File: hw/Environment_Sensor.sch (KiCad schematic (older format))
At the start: 30 parts, among them P1 CONN_4, P2 CONN_4, U1 MCP1703T, U2 PCA9512ADP, U3 TMP105, U4 HIH-6131-021, U5 MPL115A, U6 TSL2561T, U7 HTU21D

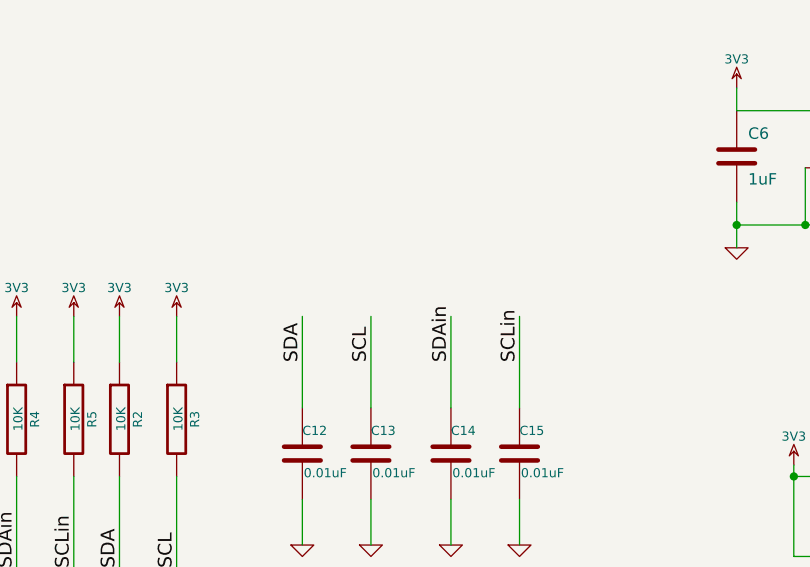
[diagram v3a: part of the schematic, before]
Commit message: Updated to add the caps on to the SDA/SCL lines
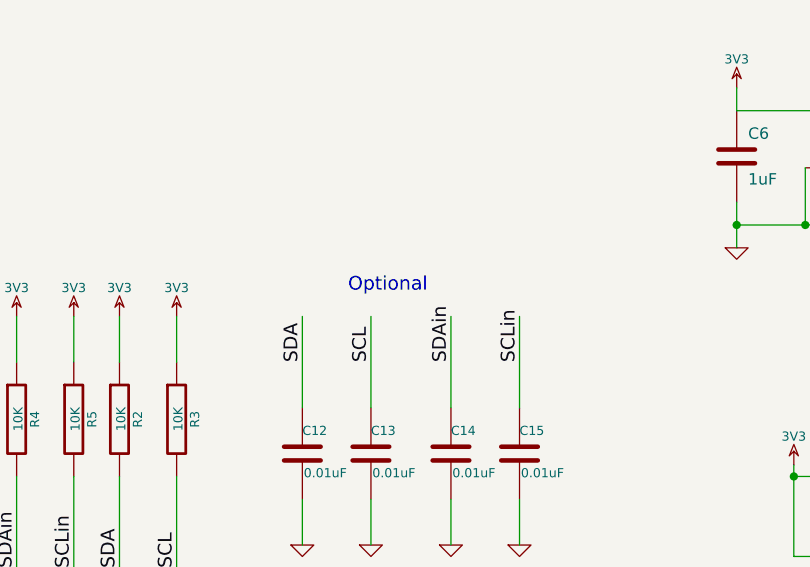
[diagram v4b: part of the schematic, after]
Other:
- note added: "Optional"
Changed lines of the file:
@@
 	5200 1650 5200 1550
 $Comp
-L +5V #PWR22
+L +5V #PWR01
 U 1 1 53729ED8
 P 5200 1550
-F 0 "#PWR22" H 5200 1640 20  0001 C CNN
+F 0 "#PWR01" H 5200 1640 20  0001 C CNN
 F 1 "+5V" H 5200 1640 30  0000 C CNN
 F 2 "" H 5200 1550 60  0001 C CNN
@@
 $EndComp
 $Comp
-L PWR_FLAG #FLG1
+L PWR_FLAG #FLG02
 U 1 1 53729EC8
 P 5200 1650
-F 0 "#FLG1" H 5200 1745 30  0001 C CNN
+F 0 "#FLG02" H 5200 1745 30  0001 C CNN
 F 1 "PWR_FLAG" H 5200 1830 30  0000 C CNN
 F 2 "" H 5200 1650 60  0001 C CNN
@@
 SDA
 $Comp
-L 3V3 #PWR28
+L 3V3 #PWR03
 U 1 1 5372962B
 P 6750 2850
-F 0 "#PWR28" H 6750 2950 40  0001 C CNN
+F 0 "#PWR03" H 6750 2950 40  0001 C CNN
 F 1 "3V3" H 6750 2975 40  0000 C CNN
 F 2 "" H 6750 2850 60  0001 C CNN
@@
 $EndComp
 $Comp
-L GND #PWR26
+L GND #PWR04
 U 1 1 537295E4
 P 6350 3350
-F 0 "#PWR26" H 6350 3350 30  0001 C CNN
+F 0 "#PWR04" H 6350 3350 30  0001 C CNN
 F 1 "GND" H 6350 3280 30  0001 C CNN
 F 2 "" H 6350 3350 60  0001 C CNN
@@
 $EndComp
 $Comp
-L 3V3 #PWR16
+L 3V3 #PWR05
 U 1 1 53729235
 P 4650 2950
-F 0 "#PWR16" H 4650 3050 40  0001 C CNN
+F 0 "#PWR05" H 4650 3050 40  0001 C CNN
 F 1 "3V3" H 4650 3075 40  0000 C CNN
 F 2 "" H 4650 2950 60  0001 C CNN
@@
 $EndComp
 $Comp
-L GND #PWR17
+L GND #PWR06
 U 1 1 5372922C
 P 4650 3500
-F 0 "#PWR17" H 4650 3500 30  0001 C CNN
+F 0 "#PWR06" H 4650 3500 30  0001 C CNN
 F 1 "GND" H 4650 3430 30  0001 C CNN
 F 2 "" H 4650 3500 60  0001 C CNN
@@
 $EndComp
 $Comp
-L GND #PWR19
+L GND #PWR07
 U 1 1 53729228
 P 4850 3450
-F 0 "#PWR19" H 4850 3450 30  0001 C CNN
+F 0 "#PWR07" H 4850 3450 30  0001 C CNN
 F 1 "GND" H 4850 3380 30  0001 C CNN
 F 2 "" H 4850 3450 60  0001 C CNN
@@
 SDA
 $Comp
-L 3V3 #PWR10
+L 3V3 #PWR08
 U 1 1 53728CA5
 P 3400 7400
-F 0 "#PWR10" H 3400 7500 40  0001 C CNN
+F 0 "#PWR08" H 3400 7500 40  0001 C CNN
 F 1 "3V3" H 3400 7525 40  0000 C CNN
 F 2 "" H 3400 7400 60  0001 C CNN
@@
 $EndComp
 $Comp
-L 3V3 #PWR1
+L 3V3 #PWR09
 U 1 1 53728C52
 P 1350 6350
-F 0 "#PWR1" H 1350 6450 40  0001 C CNN
+F 0 "#PWR09" H 1350 6450 40  0001 C CNN
 F 1 "3V3" H 1350 6475 40  0000 C CNN
 F 2 "" H 1350 6350 60  0001 C CNN
@@
 $EndComp
 $Comp
-L GND #PWR13
+L GND #PWR010
 U 1 1 53728C4C
 P 3850 6850
-F 0 "#PWR13" H 3850 6850 30  0001 C CNN
+F 0 "#PWR010" H 3850 6850 30  0001 C CNN
 F 1 "GND" H 3850 6780 30  0001 C CNN
 F 2 "" H 3850 6850 60  0001 C CNN
@@
 $EndComp
 $Comp
-L GND #PWR6
+L GND #PWR011
 U 1 1 53728C0A
 P 2000 6750
-F 0 "#PWR6" H 2000 6750 30  0001 C CNN
+F 0 "#PWR011" H 2000 6750 30  0001 C CNN
 F 1 "GND" H 2000 6680 30  0001 C CNN
 F 2 "" H 2000 6750 60  0001 C CNN
@@
 $EndComp
 $Comp
-L +5V #PWR14
+L +5V #PWR012
 U 1 1 53728BED
 P 3950 6350
-F 0 "#PWR14" H 3950 6440 20  0001 C CNN
+F 0 "#PWR012" H 3950 6440 20  0001 C CNN
 F 1 "+5V" H 3950 6440 30  0000 C CNN
 F 2 "" H 3950 6350 60  0001 C CNN
@@
 $EndComp
 $Comp
-L GND #PWR2
+L GND #PWR013
 U 1 1 53728BD6
 P 1550 6850
-F 0 "#PWR2" H 1550 6850 30  0001 C CNN
+F 0 "#PWR013" H 1550 6850 30  0001 C CNN
 F 1 "GND" H 1550 6780 30  0001 C CNN
 F 2 "" H 1550 6850 60  0001 C CNN
@@
 $EndComp
 $Comp
-L +5V #PWR3
+L +5V #PWR014
 U 1 1 537288EE
 P 1700 3850
-F 0 "#PWR3" H 1700 3940 20  0001 C CNN
+F 0 "#PWR014" H 1700 3940 20  0001 C CNN
 F 1 "+5V" H 1700 3940 30  0000 C CNN
 F 2 "" H 1700 3850 60  0001 C CNN
@@
 $EndComp
 $Comp
-L 3V3 #PWR12
+L 3V3 #PWR015
 U 1 1 537288E9
 P 3500 3900
-F 0 "#PWR12" H 3500 4000 40  0001 C CNN
+F 0 "#PWR015" H 3500 4000 40  0001 C CNN
 F 1 "3V3" H 3500 4025 40  0000 C CNN
 F 2 "" H 3500 3900 60  0001 C CNN
@@
 $EndComp
 $Comp
-L GND #PWR5
+L GND #PWR016
 U 1 1 537288DE
 P 1950 4350
-F 0 "#PWR5" H 1950 4350 30  0001 C CNN
+F 0 "#PWR016" H 1950 4350 30  0001 C CNN
 F 1 "GND" H 1950 4280 30  0001 C CNN
 F 2 "" H 1950 4350 60  0001 C CNN
@@
 $EndComp
 $Comp
-L GND #PWR8
+L GND #PWR017
 U 1 1 537288D9
 P 2600 4550
-F 0 "#PWR8" H 2600 4550 30  0001 C CNN
+F 0 "#PWR017" H 2600 4550 30  0001 C CNN
 F 1 "GND" H 2600 4480 30  0001 C CNN
 F 2 "" H 2600 4550 60  0001 C CNN
@@
 $EndComp
 $Comp
-L 3V3 #PWR36
+L 3V3 #PWR018
 U 1 1 5372789B
 P 8150 5300
-F 0 "#PWR36" H 8150 5400 40  0001 C CNN
+F 0 "#PWR018" H 8150 5400 40  0001 C CNN
 F 1 "3V3" H 8150 5425 40  0000 C CNN
 F 2 "" H 8150 5300 60  0001 C CNN
@@
 $EndComp
 $Comp
-L 3V3 #PWR31
+L 3V3 #PWR019
 U 1 1 53727880
 P 7550 4500
-F 0 "#PWR31" H 7550 4600 40  0001 C CNN
+F 0 "#PWR019" H 7550 4600 40  0001 C CNN
 F 1 "3V3" H 7550 4625 40  0000 C CNN
 F 2 "" H 7550 4500 60  0001 C CNN
@@
 $EndComp
 $Comp
-L GND #PWR32
+L GND #PWR020
 U 1 1 5372787B
 P 7550 5200
-F 0 "#PWR32" H 7550 5200 30  0001 C CNN
+F 0 "#PWR020" H 7550 5200 30  0001 C CNN
 F 1 "GND" H 7550 5130 30  0001 C CNN
 F 2 "" H 7550 5200 60  0001 C CNN
@@
 NoConn ~ 9700 5100
 $Comp
-L GND #PWR30
+L GND #PWR021
 U 1 1 537277D0
 P 7400 3500
-F 0 "#PWR30" H 7400 3500 30  0001 C CNN
+F 0 "#PWR021" H 7400 3500 30  0001 C CNN
 F 1 "GND" H 7400 3430 30  0001 C CNN
 F 2 "" H 7400 3500 60  0001 C CNN
@@
 $EndComp
 $Comp
-L 3V3 #PWR29
+L 3V3 #PWR022
 U 1 1 537277C9
 P 7400 2800
-F 0 "#PWR29" H 7400 2900 40  0001 C CNN
+F 0 "#PWR022" H 7400 2900 40  0001 C CNN
 F 1 "3V3" H 7400 2925 40  0000 C CNN
 F 2 "" H 7400 2800 60  0001 C CNN
@@
 $EndComp
 $Comp
-L 3V3 #PWR33
+L 3V3 #PWR023
 U 1 1 53727546
 P 7800 6150
-F 0 "#PWR33" H 7800 6250 40  0001 C CNN
+F 0 "#PWR023" H 7800 6250 40  0001 C CNN
 F 1 "3V3" H 7800 6275 40  0000 C CNN
 F 2 "" H 7800 6150 60  0001 C CNN
@@
 $EndComp
 $Comp
-L GND #PWR37
+L GND #PWR024
 U 1 1 5372753A
 P 8300 6600
-F 0 "#PWR37" H 8300 6600 30  0001 C CNN
+F 0 "#PWR024" H 8300 6600 30  0001 C CNN
 F 1 "GND" H 8300 6530 30  0001 C CNN
 F 2 "" H 8300 6600 60  0001 C CNN
@@
 $EndComp
 $Comp
-L +5V #PWR4
+L +5V #PWR025
 U 1 1 53726FA2
 P 1900 2100
-F 0 "#PWR4" H 1900 2190 20  0001 C CNN
+F 0 "#PWR025" H 1900 2190 20  0001 C CNN
 F 1 "+5V" H 1900 2190 30  0000 C CNN
 F 2 "" H 1900 2100 60  0001 C CNN
@@
 $EndComp
 $Comp
-L GND #PWR7
+L GND #PWR026
 U 1 1 53726F75
 P 2200 2300
-F 0 "#PWR7" H 2200 2300 30  0001 C CNN
+F 0 "#PWR026" H 2200 2300 30  0001 C CNN
 F 1 "GND" H 2200 2230 30  0001 C CNN
 F 2 "" H 2200 2300 60  0001 C CNN
@@
 	3200 2150 3200 2100
 $Comp
-L +5V #PWR9
+L +5V #PWR027
 U 1 1 539395D4
 P 3200 2100
-F 0 "#PWR9" H 3200 2190 20  0001 C CNN
+F 0 "#PWR027" H 3200 2190 20  0001 C CNN
 F 1 "+5V" H 3200 2190 30  0000 C CNN
 F 2 "" H 3200 2100 60  0001 C CNN
@@
 $EndComp
 $Comp
-L GND #PWR11
+L GND #PWR028
 U 1 1 539395DA
 P 3500 2300
-F 0 "#PWR11" H 3500 2300 30  0001 C CNN
+F 0 "#PWR028" H 3500 2300 30  0001 C CNN
 F 1 "GND" H 3500 2230 30  0001 C CNN
 F 2 "" H 3500 2300 60  0001 C CNN
@@
 	8100 1800 8100 1900
 $Comp
-L GND #PWR35
+L GND #PWR029
 U 1 1 53BB120C
 P 8100 1900
-F 0 "#PWR35" H 8100 1900 30  0001 C CNN
+F 0 "#PWR029" H 8100 1900 30  0001 C CNN
 F 1 "GND" H 8100 1830 30  0001 C CNN
 F 2 "" H 8100 1900 60  0000 C CNN
@@
 $EndComp
 $Comp
-L 3V3 #PWR34
+L 3V3 #PWR030
 U 1 1 53BB122F
 P 8100 1350
-F 0 "#PWR34" H 8100 1450 40  0001 C CNN
+F 0 "#PWR030" H 8100 1450 40  0001 C CNN
 F 1 "3V3" H 8100 1475 40  0000 C CNN
 F 2 "" H 8100 1350 60  0000 C CNN
@@
 $EndComp
 $Comp
-L 3V3 #PWR20
+L 3V3 #PWR031
 U 1 1 53D97EA8
 P 4850 5500
-F 0 "#PWR20" H 4850 5600 40  0001 C CNN
+F 0 "#PWR031" H 4850 5600 40  0001 C CNN
 F 1 "3V3" H 4850 5625 40  0000 C CNN
 F 2 "" H 4850 5500 60  0000 C CNN
@@
 $EndComp
 $Comp
-L 3V3 #PWR21
+L 3V3 #PWR032
 U 1 1 53D97EBC
 P 5100 5500
-F 0 "#PWR21" H 5100 5600 40  0001 C CNN
+F 0 "#PWR032" H 5100 5600 40  0001 C CNN
 F 1 "3V3" H 5100 5625 40  0000 C CNN
 F 2 "" H 5100 5500 60  0000 C CNN
@@
 $EndComp
 $Comp
-L GND #PWR23
+L GND #PWR033
 U 1 1 53D98156
 P 5650 6500
-F 0 "#PWR23" H 5650 6500 30  0001 C CNN
+F 0 "#PWR033" H 5650 6500 30  0001 C CNN
 F 1 "GND" H 5650 6430 30  0001 C CNN
 F 2 "" H 5650 6500 60  0000 C CNN
@@
 $EndComp
 $Comp
-L GND #PWR24
+L GND #PWR034
 U 1 1 53D9816A
 P 5950 6500
-F 0 "#PWR24" H 5950 6500 30  0001 C CNN
+F 0 "#PWR034" H 5950 6500 30  0001 C CNN
 F 1 "GND" H 5950 6430 30  0001 C CNN
 F 2 "" H 5950 6500 60  0000 C CNN
@@
 $EndComp
 $Comp
-L GND #PWR25
+L GND #PWR035
 U 1 1 53D98312
 P 6300 6500
-F 0 "#PWR25" H 6300 6500 30  0001 C CNN
+F 0 "#PWR035" H 6300 6500 30  0001 C CNN
 F 1 "GND" H 6300 6430 30  0001 C CNN
 F 2 "" H 6300 6500 60  0000 C CNN
@@
 $EndComp
 $Comp
-L GND #PWR27
+L GND #PWR036
 U 1 1 53D98318
 P 6600 6500
-F 0 "#PWR27" H 6600 6500 30  0001 C CNN
+F 0 "#PWR036" H 6600 6500 30  0001 C CNN
 F 1 "GND" H 6600 6430 30  0001 C CNN
 F 2 "" H 6600 6500 60  0000 C CNN
@@
 $EndComp
 $Comp
-L 3V3 #PWR15
+L 3V3 #PWR037
 U 1 1 53D98332
 P 4400 5500
-F 0 "#PWR15" H 4400 5600 40  0001 C CNN
+F 0 "#PWR037" H 4400 5600 40  0001 C CNN
 F 1 "3V3" H 4400 5625 40  0000 C CNN
 F 2 "" H 4400 5500 60  0000 C CNN
@@
 $EndComp
 $Comp
-L 3V3 #PWR18
+L 3V3 #PWR038
 U 1 1 53D98338
 P 4650 5500
-F 0 "#PWR18" H 4650 5600 40  0001 C CNN
+F 0 "#PWR038" H 4650 5600 40  0001 C CNN
 F 1 "3V3" H 4650 5625 40  0000 C CNN
 F 2 "" H 4650 5500 60  0000 C CNN
@@
 Wire Wire Line
 	3400 6700 3350 6700
+Text Notes 5850 5400 0    60   ~ 0
+Optional
 $EndSCHEMATC
